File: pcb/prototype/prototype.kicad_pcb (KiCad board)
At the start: 2 copper layers, 27.4 x 39 mm, 1 part

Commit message: v1 of prototype MO board
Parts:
- added C1: 1uF, prototypes:capacitor_generic, F.Cu at (45.5, 77.0)
- added D1: LED, LED_THT:LED_D5.0mm, F.Cu at (36.7, 102.0)
- added J1: SWD, prototypes:generic_3_pin, F.Cu at (65.4, 46.4)
- added J2: LOGIC_IN, prototypes:generic_4_pin, F.Cu at (61.1, 125.2)
- added J3: JMP_LOGIC, prototypes:generic_4_pin, F.Cu at (61.2, 101.5)
- added J4: JMP_GND, prototypes:generic_4_pin, F.Cu at (78.7, 112.2)
- added J5: JMP_3v3, prototypes:generic_4_pin, F.Cu at (43.7, 112.2)
- added J7: Display_power, prototypes:generic_2_pin, F.Cu at (85.3, 61.5)
- added Q1: 2N2222, prototypes:2N2222, F.Cu at (35.3, 93.2)
- added R1: 470R, Resistor_THT:R_Axial_DIN0204_L3.6mm_D1.6mm_P7.62mm_Horizontal, F.Cu at (61.5, 118.6)
- added R2: 470R, Resistor_THT:R_Axial_DIN0204_L3.6mm_D1.6mm_P7.62mm_Horizontal, F.Cu at (64.7, 118.6)
- added R3: 470R, Resistor_THT:R_Axial_DIN0204_L3.6mm_D1.6mm_P7.62mm_Horizontal, F.Cu at (67.8, 118.6)
- added R4: 470R, Resistor_THT:R_Axial_DIN0204_L3.6mm_D1.6mm_P7.62mm_Horizontal, F.Cu at (71.0, 118.6)
- added R5: 20R, Resistor_THT:R_Axial_DIN0204_L3.6mm_D1.6mm_P7.62mm_Horizontal, F.Cu at (29.6, 82.0)
- added R6: 220R, Resistor_THT:R_Axial_DIN0204_L3.6mm_D1.6mm_P7.62mm_Horizontal, F.Cu at (46.8, 87.8)
- added RPI_40Pin_breakout1: ~, prototypes:RPI_breakout_flipped, F.Cu at (86.9, 55.8)
- added S1: ~, prototypes:VS1838B, F.Cu at (46.6, 82.8)
- moved nRF52840_dk1 80.5 mm to (54.8, 54.8)
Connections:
- nRF52840_dk1 pad 1: unconnected-(nRF52840_dk1-SWDIO-Pad1) -> /DIO
- nRF52840_dk1 pad 10: unconnected-(nRF52840_dk1-0.09-Pad10) -> MOD2
- nRF52840_dk1 pad 11: unconnected-(nRF52840_dk1-0.10-Pad11) -> MOD3
- nRF52840_dk1 pad 12: unconnected-(nRF52840_dk1-1.10-Pad12) -> IR_TX
- nRF52840_dk1 pad 13: unconnected-(nRF52840_dk1-1.13-Pad13) -> IR_RX
- nRF52840_dk1 pad 14: unconnected-(nRF52840_dk1-1.15-Pad14) -> U0_TX
- nRF52840_dk1 pad 15: unconnected-(nRF52840_dk1-0.02-Pad15) -> U0_RX
- nRF52840_dk1 pad 16: unconnected-(nRF52840_dk1-0.29-Pad16) -> U1_RX
- nRF52840_dk1 pad 17: unconnected-(nRF52840_dk1-0.31-Pad17) -> U1_TX
- nRF52840_dk1 pad 18: unconnected-(nRF52840_dk1-GND-Pad18) -> GND
- nRF52840_dk1 pad 19: unconnected-(nRF52840_dk1-GND-Pad19) -> GND
- nRF52840_dk1 pad 2: unconnected-(nRF52840_dk1-SWDCLK-Pad2) -> /CLK
- nRF52840_dk1 pad 21: unconnected-(nRF52840_dk1-VBUS-Pad21) -> VBUS
- nRF52840_dk1 pad 22: unconnected-(nRF52840_dk1-VDD_OUT-Pad22) -> +1V35
- nRF52840_dk1 pad 3: unconnected-(nRF52840_dk1-0.13-Pad3) -> LOGIC0
- nRF52840_dk1 pad 4: unconnected-(nRF52840_dk1-0.15-Pad4) -> LOGIC1
- nRF52840_dk1 pad 5: unconnected-(nRF52840_dk1-0.17-Pad5) -> LOGIC2
- nRF52840_dk1 pad 6: unconnected-(nRF52840_dk1-0.20-Pad6) -> LOGIC3
- nRF52840_dk1 pad 7: unconnected-(nRF52840_dk1-0.22-Pad7) -> MOD0
- nRF52840_dk1 pad 8: unconnected-(nRF52840_dk1-0.24-Pad8) -> MOD1
- nRF52840_dk1 pad 9: unconnected-(nRF52840_dk1-1.00-Pad9) -> nRESET
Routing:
- net U1_RX: track 0.00 -> 111.7 mm
- net +3V3: track 0.00 -> 101.9 mm
- net U1_TX: track 0.00 -> 95.1 mm
- net LOGIC0: track 0.00 -> 51.6 mm
- net U0_RX: track 0.00 -> 49.2 mm
- net LOGIC1: track 0.00 -> 47.4 mm
- net U0_TX: track 0.00 -> 45.4 mm
- net VBUS: track 0.00 -> 43.6 mm
- net LOGIC2: track 0.00 -> 43.6 mm
- net GND: track 0.00 -> 40.5 mm, vias 0 -> 6
- net LOGIC3: track 0.00 -> 40.2 mm
- net /DIO: track 0.00 -> 22.2 mm, vias 0 -> 2
- net MOD3: track 0.00 -> 17.4 mm
- net nRESET: track 0.00 -> 17.4 mm
- net MOD2: track 0.00 -> 17.4 mm
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- added copper zone on F.Cu, net +3V3
- added copper zone on F.Cu, net GND
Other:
- board size 27.4 x 39 mm -> 89 x 159.3 mm

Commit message: Finish prototype circuit board
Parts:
- D1: footprint LED_THT:LED_D5.0mm -> prototypes:LED_D5.0mm
- R1, R2, R3, R4, R5, R6: footprint Resistor_THT:R_Axial_DIN0204_L3.6mm_D1.6mm_P7.62mm_Horizontal -> prototypes:resistor_tht
- moved R5 31.4 mm to (49.9, 106.0), turned to 90 degrees
- moved J1 17.6 mm to (48.2, 49.9), turned to -90 degrees
- moved J7 16.2 mm to (73.2, 50.8), turned to 0 degrees
- moved RPI_40Pin_breakout1 14.1 mm to (85.1, 41.8)
- moved S1 6.78 mm to (53.2, 84.5)
- moved C1 6.21 mm to (50.9, 80.2)
- moved D1 6.05 mm to (41.5, 98.3), turned to 0 degrees
- moved Q1 5.15 mm to (40.1, 91.3)
- moved R6 4.79 mm to (51.6, 88.0)
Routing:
- net GND: track 40.5 -> 117.5 mm, vias 6 -> 12
- net +3V3: track 101.9 -> 132.2 mm
- net /DIO: track 22.2 -> 32.9 mm
- net Net-(D1-A): track 14.3 -> 5.87 mm
- net IR_RX: track 11.7 -> 4.47 mm
- net U1_TX: track 95.1 -> 101.1 mm
- net MOD1: track 16.5 -> 21.8 mm
- net MOD0: track 16.5 -> 21.8 mm
- net IR_TX: track 10.5 -> 5.75 mm
- net U1_RX: track 111.7 -> 115.9 mm
- net /CLK: track 16.8 -> 20.4 mm
- net MOD2: track 17.4 -> 20.7 mm
- net nRESET: track 17.4 -> 20.7 mm
- net MOD3: track 17.4 -> 20.5 mm
- net U0_RX: track 49.2 -> 46.8 mm
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
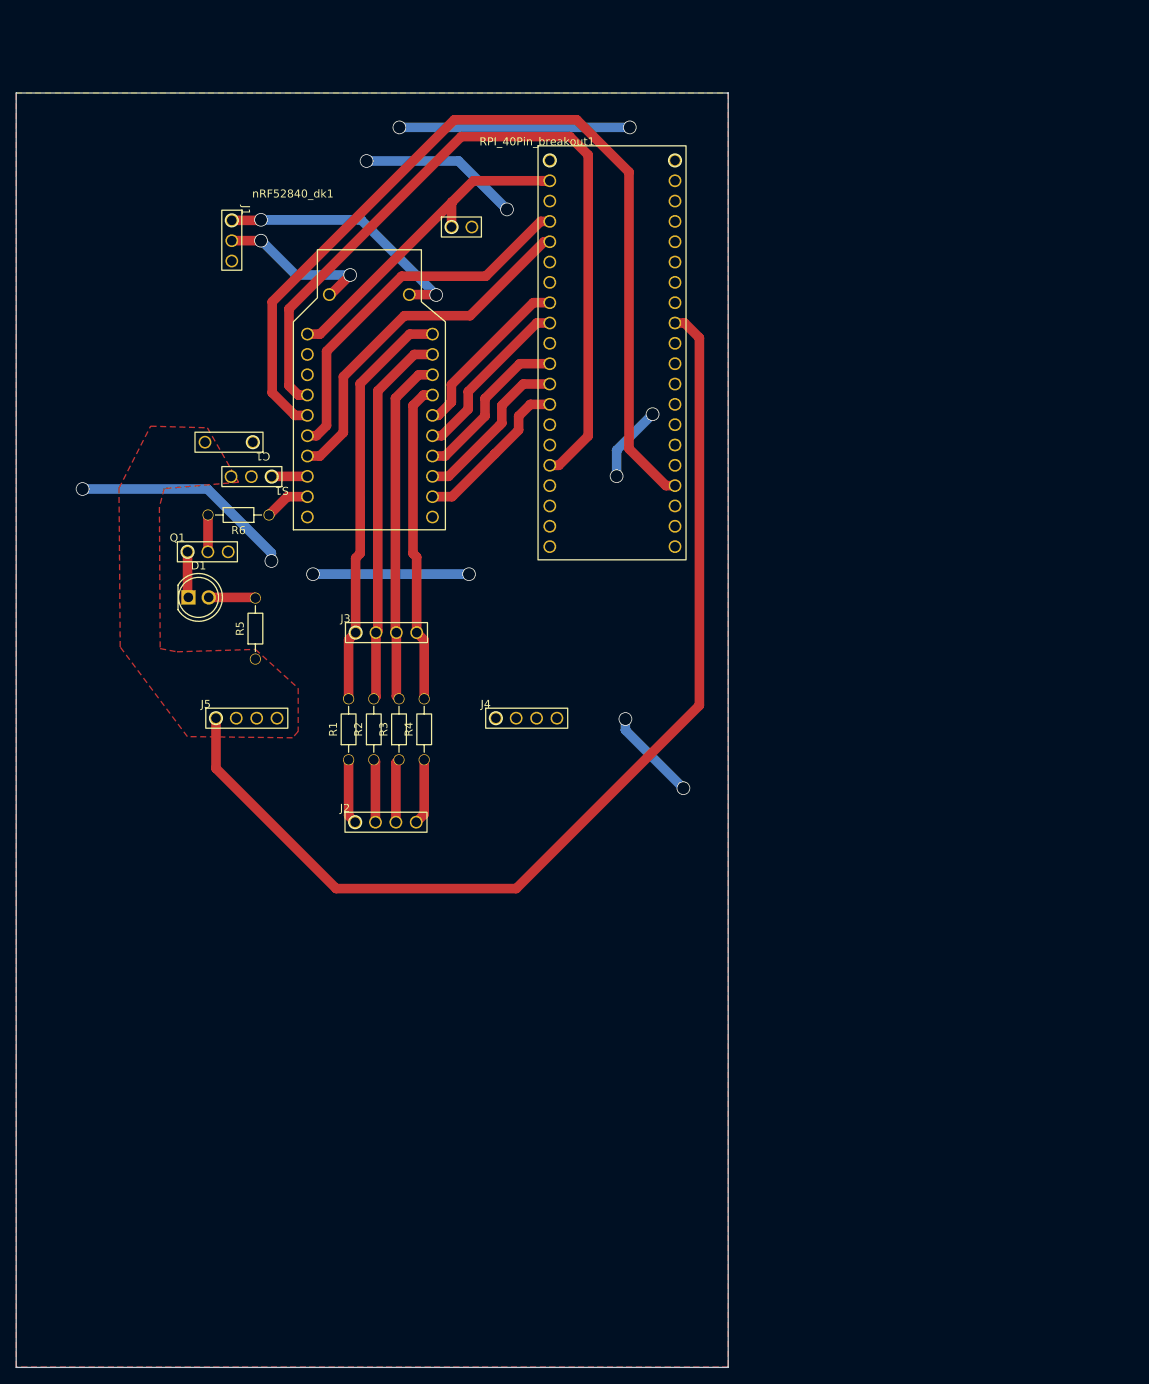
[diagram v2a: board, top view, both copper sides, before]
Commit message: Complete re-write of the firmware for new program select
Implemented a new 4 wire program select + 1 wire reset system where the
raspberry pi can put the firmware into a specific mode rather than
issuing commands.

Currently the IR subsystem is implemented in this mode, more to come
when I catch up on the PCB side.
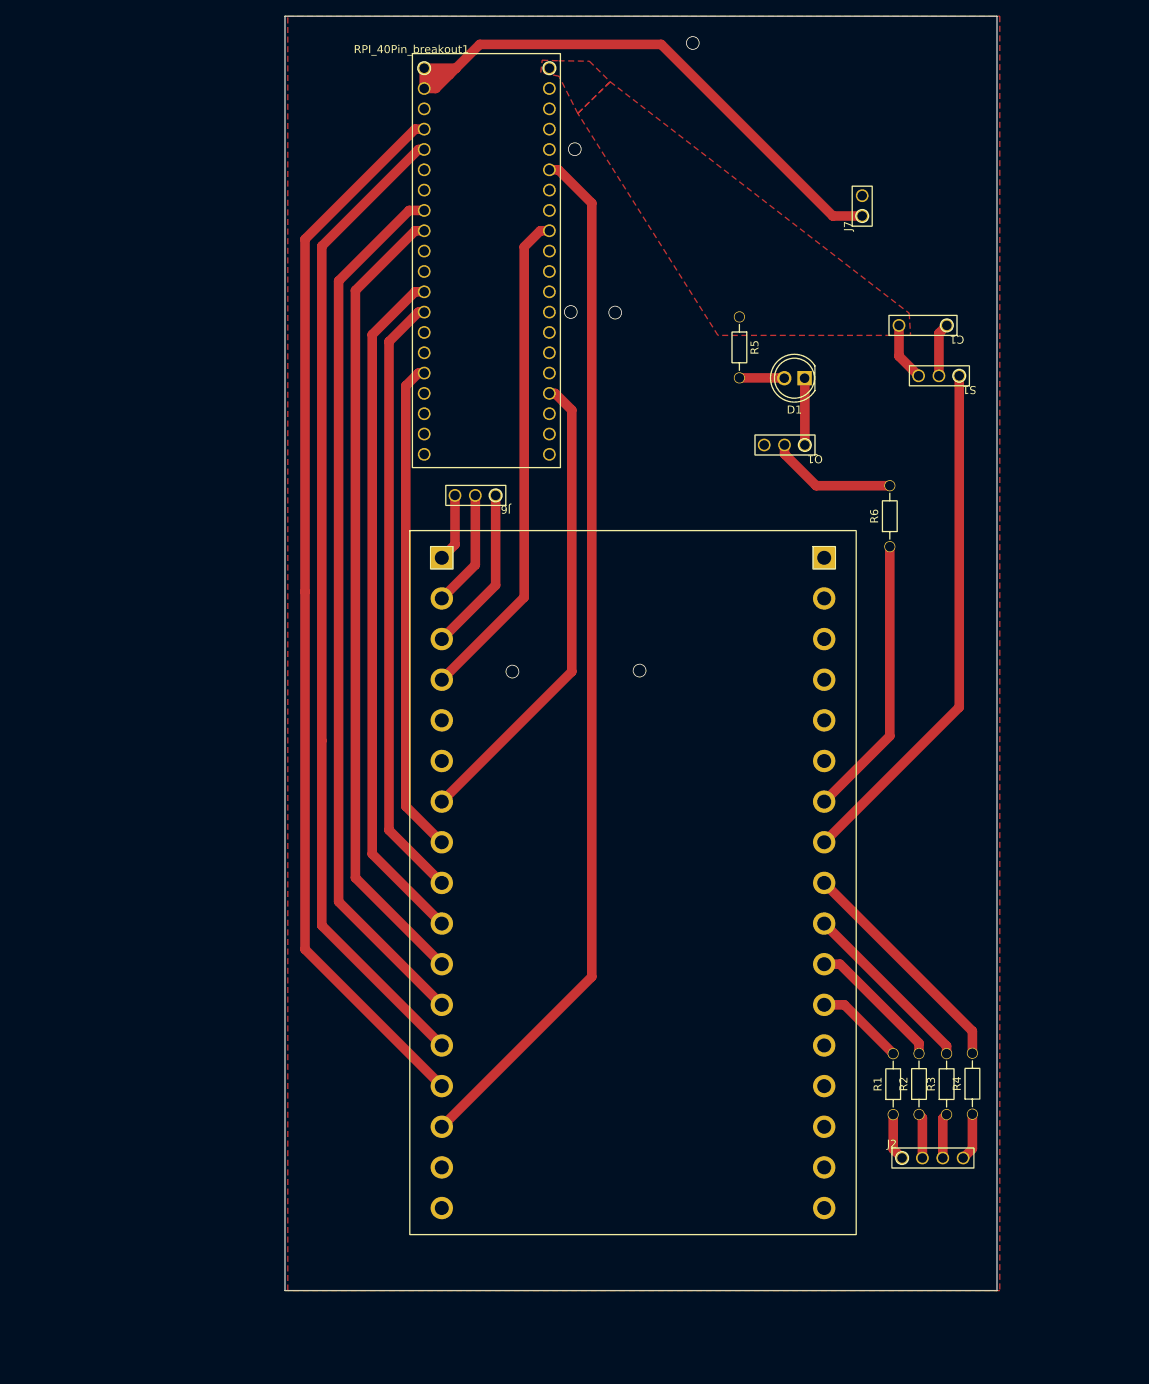
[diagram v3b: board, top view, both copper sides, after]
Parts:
- removed J1: SWD, prototypes:generic_3_pin
- removed J3: JMP_LOGIC, prototypes:generic_4_pin
- removed J4: JMP_GND, prototypes:generic_4_pin
- removed J5: JMP_3v3, prototypes:generic_4_pin
- removed nRF52840_dk1: ~, prototypes:nRF52840dk_flipped
- added J6: SWD, prototypes:generic_3_pin, F.Cu at (81.2, 86.8)
- added U1: ~, prototypes:TH-0-PDB_flipped, F.Cu at (69.0, 90.0)
- moved C1 88.0 mm to (137.6, 65.5)
- moved S1 86.9 mm to (139.2, 71.8)
- moved D1 81.8 mm to (118.5, 70.9), turned to 180 degrees
- moved R4 81.6 mm to (139.5, 162.9)
- moved R3 81.6 mm to (136.3, 162.9)
- moved R2 81.3 mm to (132.8, 162.9)
- moved R1 81.2 mm to (129.6, 162.9)
- moved Q1 80.4 mm to (119.8, 80.5), turned to 180 degrees
- moved J2 80.2 mm to (129.5, 167.1)
- moved R6 77.7 mm to (129.2, 92.0), turned to 90 degrees
- moved R5 74.1 mm to (110.4, 63.2), turned to -90 degrees
- moved J7 51.4 mm to (124.5, 51.9), turned to 90 degrees
- moved RPI_40Pin_breakout1 19.5 mm to (69.4, 30.3)
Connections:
- RPI_40Pin_breakout1 pad 11: unconnected-(RPI_40Pin_breakout1-GPIO17-Pad11) -> nRESET
- RPI_40Pin_breakout1 pad 20: unconnected-(RPI_40Pin_breakout1-GND-Pad20) -> GND
- RPI_40Pin_breakout1 pad 22: nRESET -> unconnected-(RPI_40Pin_breakout1-GPIO25-Pad22)
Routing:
- net GND: track 117.5 -> 6.99 mm, vias 12 -> 6
- net nRESET: track 20.7 -> 130.2 mm
- net MOD0: track 21.8 -> 110.2 mm
- net U0_RX: track 46.8 -> 133.5 mm
- net MOD1: track 21.8 -> 100.4 mm
- net U0_TX: track 45.5 -> 123.9 mm
- net MOD2: track 20.7 -> 85.9 mm
- net +3V3: track 132.2 -> 69.7 mm
- net IR_RX: track 4.47 -> 65.3 mm
- net U1_RX: track 115.9 -> 59.3 mm
- net MOD3: track 20.5 -> 76.3 mm
- net LOGIC0: track 51.6 -> 11.2 mm
- net U1_TX: track 101.1 -> 61.9 mm
- net VBUS: track 42.5 -> 76.2 mm
- net LOGIC1: track 47.4 -> 17.2 mm
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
